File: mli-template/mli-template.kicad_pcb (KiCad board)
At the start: 2 copper layers, 106.6 x 125.6 mm, 0 parts

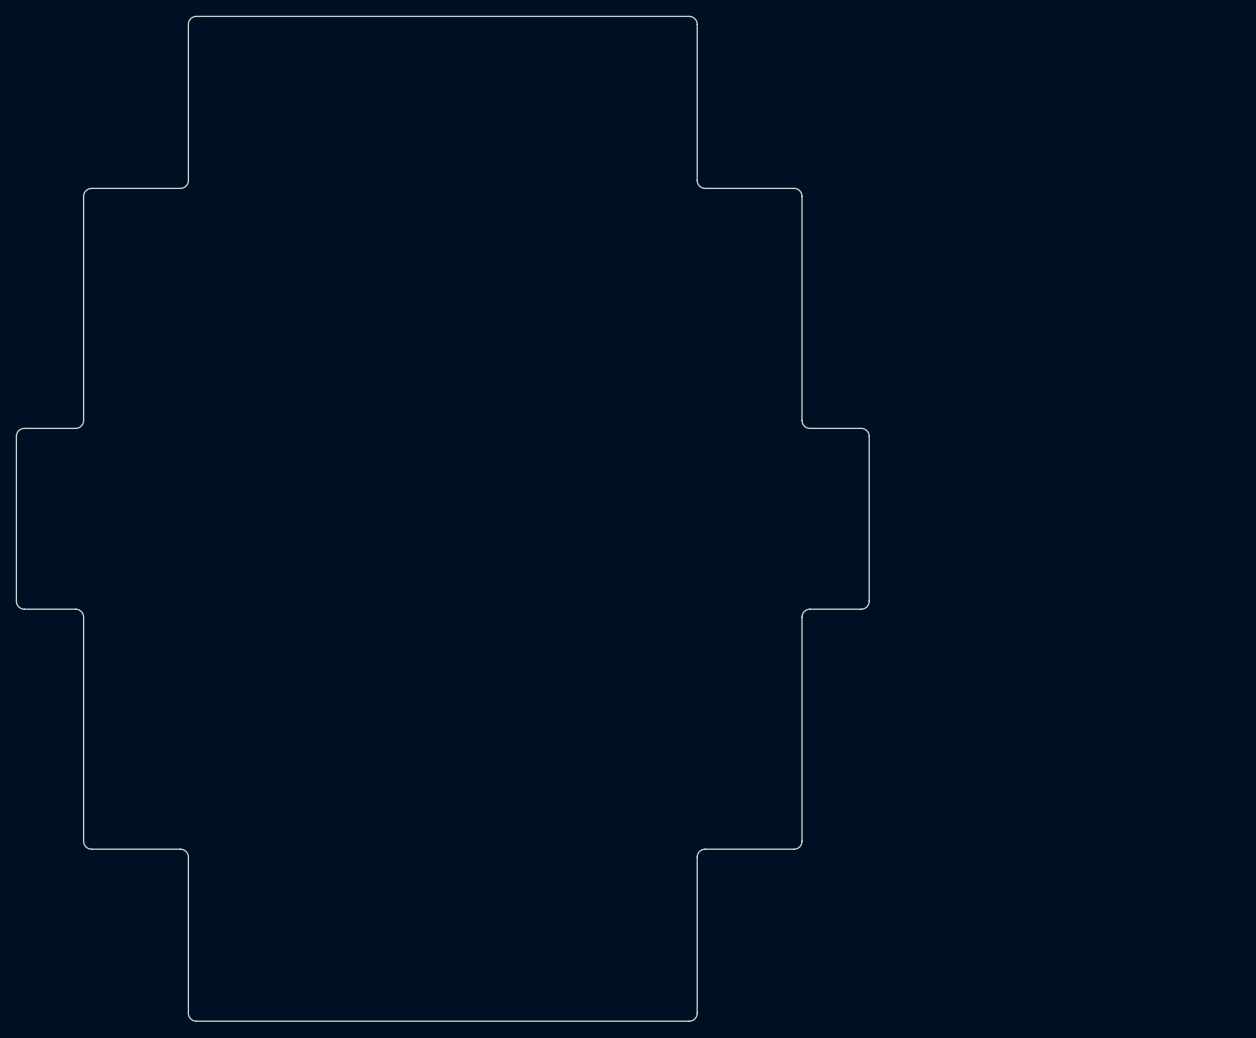
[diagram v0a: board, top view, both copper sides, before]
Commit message: Expanded a few mm to catch more battery area
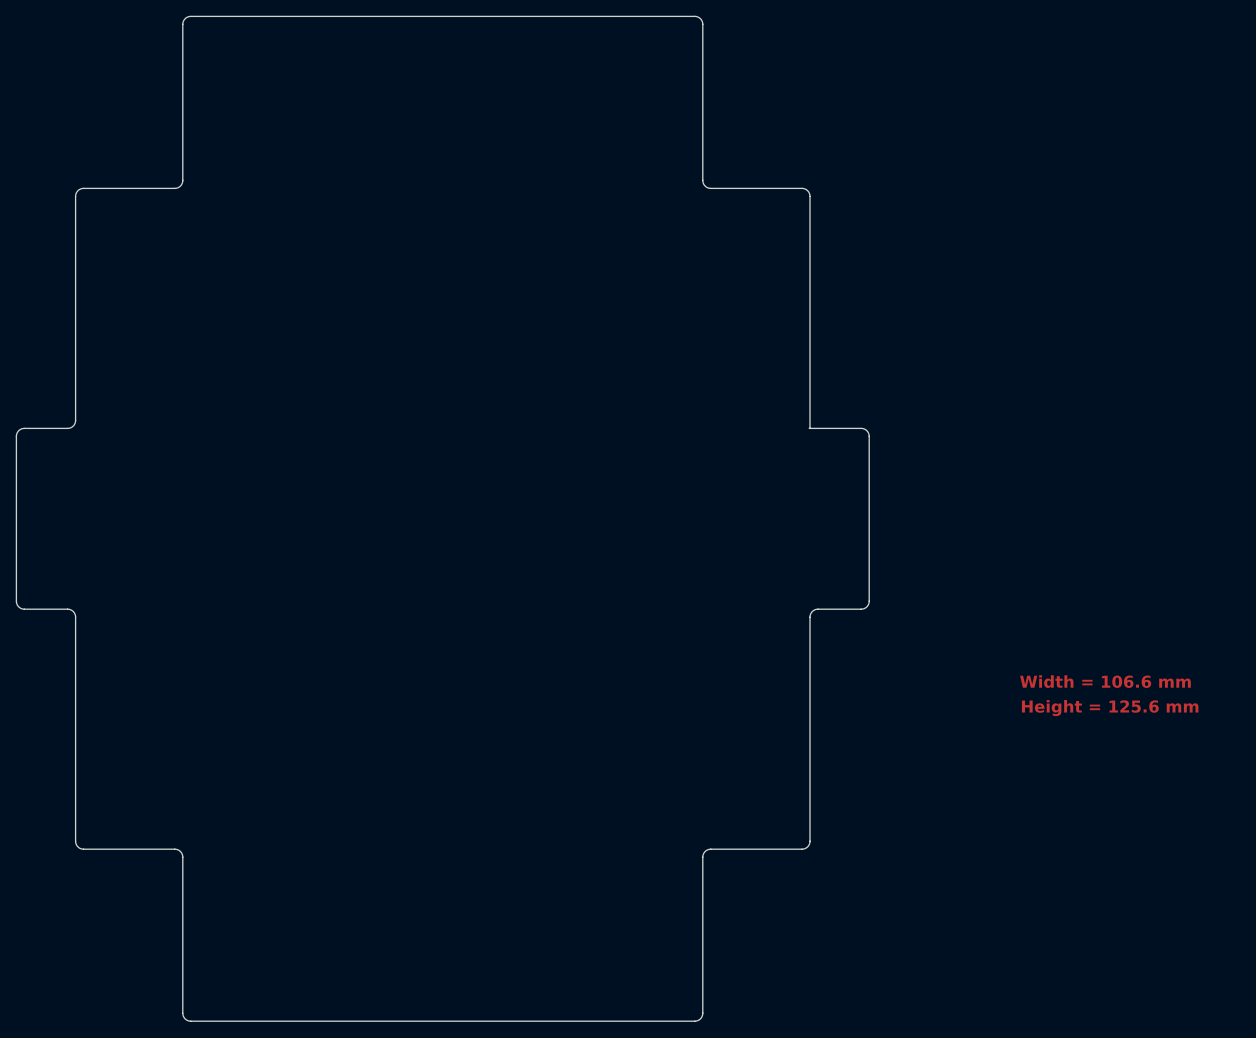
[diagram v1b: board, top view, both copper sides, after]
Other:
- outline, holes or cut-outs redrawn
- board text added: "Height = 125.6 mm"
- board text added: "Width = 106.6 mm"
- board text removed: "All corners radiused 1 mm"

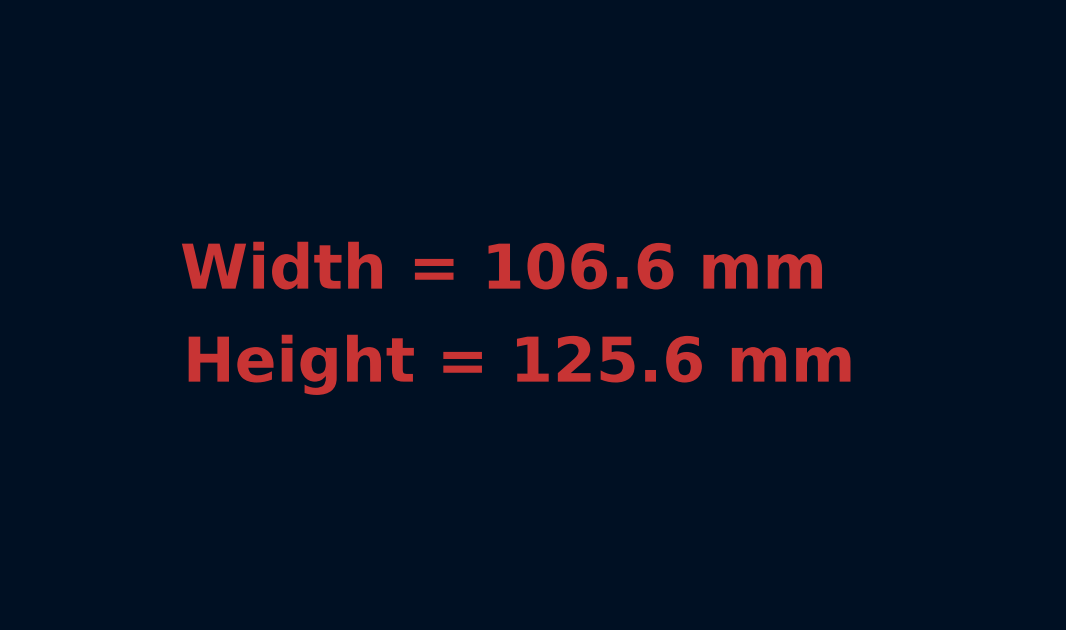
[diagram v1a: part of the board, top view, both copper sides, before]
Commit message: Add some external dimensions
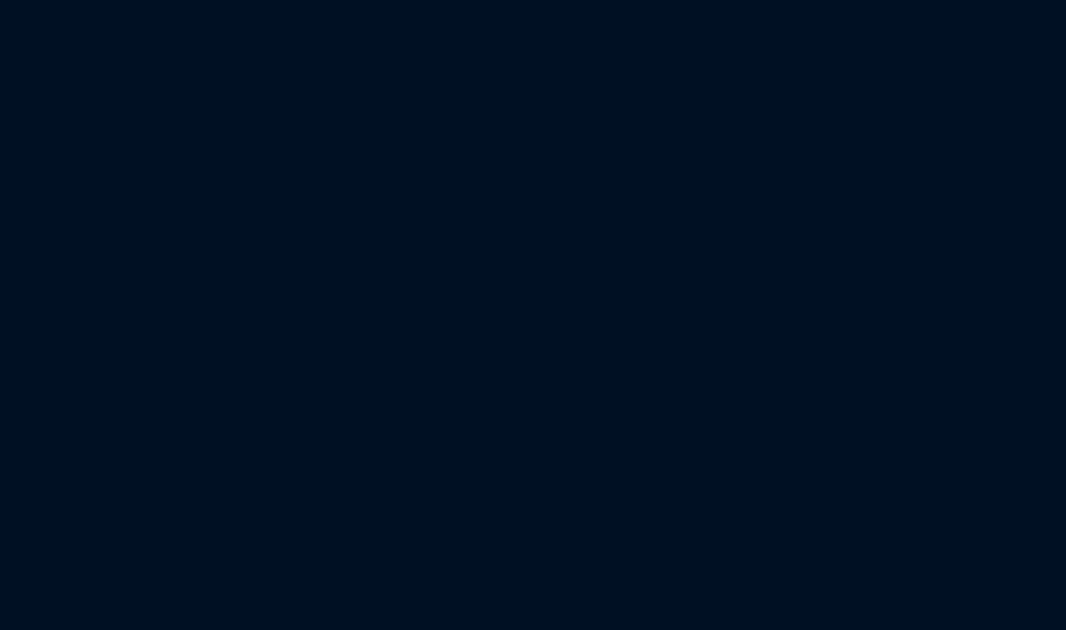
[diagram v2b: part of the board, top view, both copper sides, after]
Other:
- board text removed: "Height = 125.6 mm"
- board text removed: "Width = 106.6 mm"
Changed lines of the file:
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@@
   (gr_line (start 161.3 63) (end 161.3 145.6)
     (stroke (width 0.1) (type default)) (layer "F.Fab"))
-  (gr_text "Height = 125.6 mm" (at 200 128.7) (layer "F.Cu")
-    (effects (font (size 1.5 1.5) (thickness 0.3) bold) (justify left bottom))
+  (dimension (type aligned) (layer "User.4")
+    (pts (xy 74.5 93) (xy 181.1 93))
+    (height -59.575635)
+    (gr_text "106.6000 mm" (at 127.8 33.424365) (layer "User.4")
+      (effects (font (size 1 1) (thickness 0.15)))
+    )
+    (format (prefix "") (suffix "") (units 3) (units_format 1) (precision 4))
+    (style (thickness 0.15) (arrow_length 1.27) (text_position_mode 1) (extension_height 0.58642) (extension_offset 10) keep_text_aligned)
   )
-  (gr_text "Width = 106.6 mm" (at 199.9 125.6) (layer "F.Cu")
-    (effects (font (size 1.5 1.5) (thickness 0.3) bold) (justify left bottom))
+  (dimension (type aligned) (layer "User.4")
+    (pts (xy 127.8 41.5) (xy 127.8 167.1))
+    (height 72.4)
+    (gr_text "125.6000 mm" (at 55.4 104.3 90) (layer "User.4")
+      (effects (font (size 1 1) (thickness 0.15)))
+    )
+    (format (prefix "") (suffix "") (units 3) (units_format 1) (precision 4))
+    (style (thickness 0.15) (arrow_length 1.27) (text_position_mode 1) (extension_height 0.58642) (extension_offset 40) keep_text_aligned)
   )
 )
